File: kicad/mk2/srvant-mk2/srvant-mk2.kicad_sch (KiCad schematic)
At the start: 0 parts

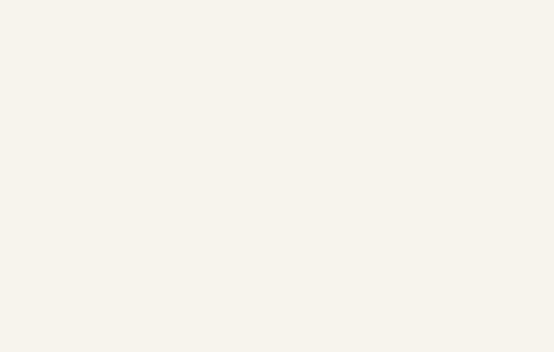
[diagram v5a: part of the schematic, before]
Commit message: mostly wired, impedance control, etc
Repositioned most of the components. Set impedance control based
on jlcpcb calculator.

Need to:
* reposition ethernet port to allow mounting hole.
* move power socket lower, reduce board size
* fix the rest of DRC errors.
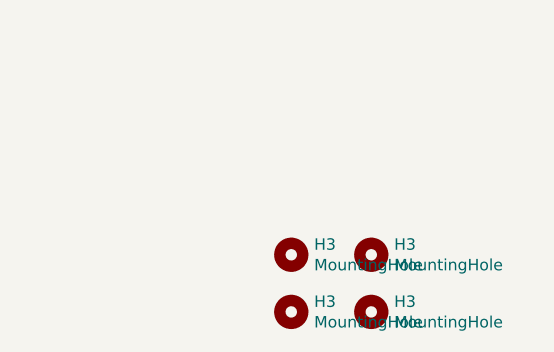
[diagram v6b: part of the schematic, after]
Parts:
- added H3 (x4): MountingHole, MountingHole:MountingHole_2.5mm_Pad_TopOnly, symbol Mechanical:MountingHole
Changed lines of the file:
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@@
     (effects (font (size 1.27 1.27)) (justify left bottom))
+  )
+  (symbol (lib_id "Mechanical:MountingHole") (at 392.43 240.03 0) (unit 1)
+    (in_bom yes) (on_board yes) (dnp no)
+    (property "Reference" "H3" (at 394.97 238.887 0)
+      (effects (font (size 1.27 1.27)) (justify left))
+    )
+    (property "Value" "MountingHole" (at 394.97 241.173 0)
+      (effects (font (size 1.27 1.27)) (justify left))
+    )
+    (property "Footprint" "MountingHole:MountingHole_2.5mm_Pad_TopOnly" (at 392.43 240.03 0)
+      (effects (font (size 1.27 1.27)) hide)
+    )
+    (property "Datasheet" "~{}" (at 392.43 240.03 0)
+      (effects (font (size 1.27 1.27)) hide)
+    )
+    (property "Field4" "nf" (at 392.43 240.03 0)
+      (effects (font (size 1.27 1.27)) hide)
+    )
+    (property "Field5" "nf" (at 392.43 240.03 0)
+      (effects (font (size 1.27 1.27)) hide)
+    )
+    (property "Field6" "nf" (at 392.43 240.03 0)
+      (effects (font (size 1.27 1.27)) hide)
+    )
+    (property "Field7" "nf" (at 392.43 240.03 0)
+      (effects (font (size 1.27 1.27)) hide)
+    )
+    (property "Part Description" "M2.5 mounting hole" (at 392.43 240.03 0)
+      (effects (font (size 1.27 1.27)) hide)
+    )
+    (instances
+      (project "srvant-mk2"
+        (path "/1859a578-b791-4142-bdf4-fda494df1146/75d0860a-7ab5-4d7d-b96d-9266ebc33987"
+          (reference "H3") (unit 1)
+        )
+        (path "/1859a578-b791-4142-bdf4-fda494df1146"
+          (reference "H7") (unit 1)
+        )
+      )
+      (project "srvant"
+        (path "/556fa623-1b37-4e79-bae4-da8a8b5c51e2/e09acda0-94a3-4a08-aefe-d9a65d235818/b80aa315-5e9f-46e9-a408-0a475f97171d"
+          (reference "H10") (unit 1)
+        )
+      )
+    )
+  )
+  (symbol (lib_id "Mechanical:MountingHole") (at 401.32 246.38 0) (unit 1)
+    (in_bom yes) (on_board yes) (dnp no)
+    (property "Reference" "H3" (at 403.86 245.237 0)
+      (effects (font (size 1.27 1.27)) (justify left))
+    )
+    (property "Value" "MountingHole" (at 403.86 247.523 0)
+      (effects (font (size 1.27 1.27)) (justify left))
+    )
+    (property "Footprint" "MountingHole:MountingHole_2.5mm_Pad_TopOnly" (at 401.32 246.38 0)
+      (effects (font (size 1.27 1.27)) hide)
+    )
+    (property "Datasheet" "~{}" (at 401.32 246.38 0)
+      (effects (font (size 1.27 1.27)) hide)
+    )
+    (property "Field4" "nf" (at 401.32 246.38 0)
+      (effects (font (size 1.27 1.27)) hide)
+    )
+    (property "Field5" "nf" (at 401.32 246.38 0)
+      (effects (font (size 1.27 1.27)) hide)
+    )
+    (property "Field6" "nf" (at 401.32 246.38 0)
+      (effects (font (size 1.27 1.27)) hide)
+    )
+    (property "Field7" "nf" (at 401.32 246.38 0)
+      (effects (font (size 1.27 1.27)) hide)
+    )
+    (property "Part Description" "M2.5 mounting hole" (at 401.32 246.38 0)
+      (effects (font (size 1.27 1.27)) hide)
+    )
+    (instances
+      (project "srvant-mk2"
+        (path "/1859a578-b791-4142-bdf4-fda494df1146/75d0860a-7ab5-4d7d-b96d-9266ebc33987"
+          (reference "H3") (unit 1)
+        )
+        (path "/1859a578-b791-4142-bdf4-fda494df1146"
+          (reference "H4") (unit 1)
+        )
+      )
+      (project "srvant"
+        (path "/556fa623-1b37-4e79-bae4-da8a8b5c51e2/e09acda0-94a3-4a08-aefe-d9a65d235818/b80aa315-5e9f-46e9-a408-0a475f97171d"
+          (reference "H10") (unit 1)
+        )
+      )
+    )
+  )
+  (symbol (lib_id "Mechanical:MountingHole") (at 401.32 240.03 0) (unit 1)
+    (in_bom yes) (on_board yes) (dnp no)
+    (property "Reference" "H3" (at 403.86 238.887 0)
+      (effects (font (size 1.27 1.27)) (justify left))
+    )
+    (property "Value" "MountingHole" (at 403.86 241.173 0)
+      (effects (font (size 1.27 1.27)) (justify left))
+    )
+    (property "Footprint" "MountingHole:MountingHole_2.5mm_Pad_TopOnly" (at 401.32 240.03 0)
+      (effects (font (size 1.27 1.27)) hide)
+    )
+    (property "Datasheet" "~{}" (at 401.32 240.03 0)
+      (effects (font (size 1.27 1.27)) hide)
+    )
+    (property "Field4" "nf" (at 401.32 240.03 0)
+      (effects (font (size 1.27 1.27)) hide)
+    )
+    (property "Field5" "nf" (at 401.32 240.03 0)
+      (effects (font (size 1.27 1.27)) hide)
+    )
+    (property "Field6" "nf" (at 401.32 240.03 0)
+      (effects (font (size 1.27 1.27)) hide)
+    )
+    (property "Field7" "nf" (at 401.32 240.03 0)
+      (effects (font (size 1.27 1.27)) hide)
+    )
+    (property "Part Description" "M2.5 mounting hole" (at 401.32 240.03 0)
+      (effects (font (size 1.27 1.27)) hide)
+    )
+    (instances
+      (project "srvant-mk2"
+        (path "/1859a578-b791-4142-bdf4-fda494df1146/75d0860a-7ab5-4d7d-b96d-9266ebc33987"
+          (reference "H3") (unit 1)
+        )
+        (path "/1859a578-b791-4142-bdf4-fda494df1146"
+          (reference "H6") (unit 1)
+        )
+      )
+      (project "srvant"
+        (path "/556fa623-1b37-4e79-bae4-da8a8b5c51e2/e09acda0-94a3-4a08-aefe-d9a65d235818/b80aa315-5e9f-46e9-a408-0a475f97171d"
+          (reference "H10") (unit 1)
+        )
+      )
+    )
+  )
+  (symbol (lib_id "Mechanical:MountingHole") (at 392.43 246.38 0) (unit 1)
+    (in_bom yes) (on_board yes) (dnp no)
+    (property "Reference" "H3" (at 394.97 245.237 0)
+      (effects (font (size 1.27 1.27)) (justify left))
+    )
+    (property "Value" "MountingHole" (at 394.97 247.523 0)
+      (effects (font (size 1.27 1.27)) (justify left))
+    )
+    (property "Footprint" "MountingHole:MountingHole_2.5mm_Pad_TopOnly" (at 392.43 246.38 0)
+      (effects (font (size 1.27 1.27)) hide)
+    )
+    (property "Datasheet" "~{}" (at 392.43 246.38 0)
+      (effects (font (size 1.27 1.27)) hide)
+    )
+    (property "Field4" "nf" (at 392.43 246.38 0)
+      (effects (font (size 1.27 1.27)) hide)
+    )
+    (property "Field5" "nf" (at 392.43 246.38 0)
+      (effects (font (size 1.27 1.27)) hide)
+    )
+    (property "Field6" "nf" (at 392.43 246.38 0)
+      (effects (font (size 1.27 1.27)) hide)
+    )
+    (property "Field7" "nf" (at 392.43 246.38 0)
+      (effects (font (size 1.27 1.27)) hide)
+    )
+    (property "Part Description" "M2.5 mounting hole" (at 392.43 246.38 0)
+      (effects (font (size 1.27 1.27)) hide)
+    )
+    (instances
+      (project "srvant-mk2"
+        (path "/1859a578-b791-4142-bdf4-fda494df1146/75d0860a-7ab5-4d7d-b96d-9266ebc33987"
+          (reference "H3") (unit 1)
+        )
+        (path "/1859a578-b791-4142-bdf4-fda494df1146"
+          (reference "H5") (unit 1)
+        )
+      )
+      (project "srvant"
+        (path "/556fa623-1b37-4e79-bae4-da8a8b5c51e2/e09acda0-94a3-4a08-aefe-d9a65d235818/b80aa315-5e9f-46e9-a408-0a475f97171d"
+          (reference "H10") (unit 1)
+        )
+      )
+    )
   )
   (sheet (at 262.89 95.25) (size 68.58 81.28) (fields_autoplaced)

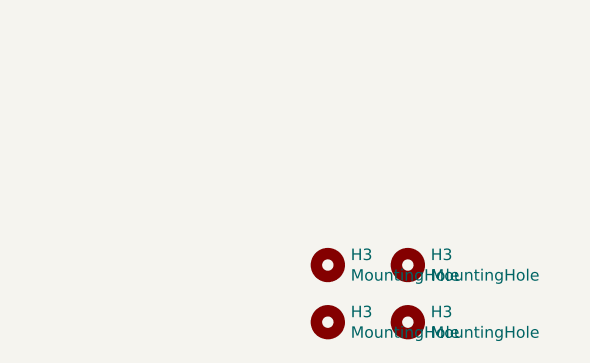
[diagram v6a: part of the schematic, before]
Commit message: add rp-t113-s3 datasheets (cn), make CI happier
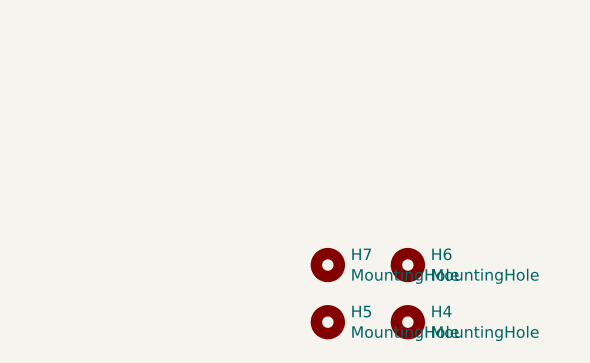
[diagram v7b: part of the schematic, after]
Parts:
- renumbered H3 to H4, H3 to H5, H3 to H6, H3 to H7
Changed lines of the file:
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@@
   (symbol (lib_id "Mechanical:MountingHole") (at 392.43 240.03 0) (unit 1)
     (in_bom yes) (on_board yes) (dnp no)
-    (property "Reference" "H3" (at 394.97 238.887 0)
+    (property "Reference" "H7" (at 394.97 238.887 0)
       (effects (font (size 1.27 1.27)) (justify left))
     )
@@
     (instances
       (project "srvant-mk2"
-        (path "/1859a578-b791-4142-bdf4-fda494df1146/75d0860a-7ab5-4d7d-b96d-9266ebc33987"
-          (reference "H3") (unit 1)
-        )
         (path "/1859a578-b791-4142-bdf4-fda494df1146"
           (reference "H7") (unit 1)
@@
   (symbol (lib_id "Mechanical:MountingHole") (at 401.32 246.38 0) (unit 1)
     (in_bom yes) (on_board yes) (dnp no)
-    (property "Reference" "H3" (at 403.86 245.237 0)
+    (property "Reference" "H4" (at 403.86 245.237 0)
       (effects (font (size 1.27 1.27)) (justify left))
     )
@@
     (instances
       (project "srvant-mk2"
-        (path "/1859a578-b791-4142-bdf4-fda494df1146/75d0860a-7ab5-4d7d-b96d-9266ebc33987"
-          (reference "H3") (unit 1)
-        )
         (path "/1859a578-b791-4142-bdf4-fda494df1146"
           (reference "H4") (unit 1)
@@
   (symbol (lib_id "Mechanical:MountingHole") (at 401.32 240.03 0) (unit 1)
     (in_bom yes) (on_board yes) (dnp no)
-    (property "Reference" "H3" (at 403.86 238.887 0)
+    (property "Reference" "H6" (at 403.86 238.887 0)
       (effects (font (size 1.27 1.27)) (justify left))
     )
@@
     (instances
       (project "srvant-mk2"
-        (path "/1859a578-b791-4142-bdf4-fda494df1146/75d0860a-7ab5-4d7d-b96d-9266ebc33987"
-          (reference "H3") (unit 1)
-        )
         (path "/1859a578-b791-4142-bdf4-fda494df1146"
           (reference "H6") (unit 1)
@@
   (symbol (lib_id "Mechanical:MountingHole") (at 392.43 246.38 0) (unit 1)
     (in_bom yes) (on_board yes) (dnp no)
-    (property "Reference" "H3" (at 394.97 245.237 0)
+    (property "Reference" "H5" (at 394.97 245.237 0)
       (effects (font (size 1.27 1.27)) (justify left))
     )
@@
     (instances
       (project "srvant-mk2"
-        (path "/1859a578-b791-4142-bdf4-fda494df1146/75d0860a-7ab5-4d7d-b96d-9266ebc33987"
-          (reference "H3") (unit 1)
-        )
         (path "/1859a578-b791-4142-bdf4-fda494df1146"
           (reference "H5") (unit 1)
